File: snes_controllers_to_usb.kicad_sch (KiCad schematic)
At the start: 30 parts, among them J1 SNES_controller_port, J2 SNES_controller_port, J3 SNES_controller_port, J4 SNES_controller_port, Q1 BSS123, SW1 RST_PUSH, U1 PicoW

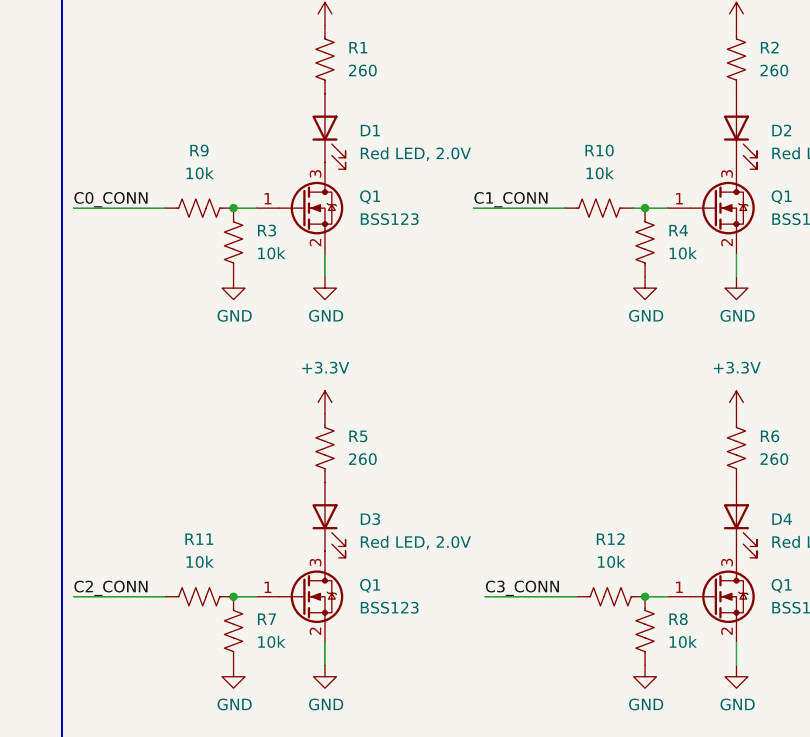
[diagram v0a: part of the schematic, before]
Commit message: Change transistor gate resistors to 1kOhm
 - Currently by using both 10kOhm resistors for pulldown and the current
   limiting resistor, it effectively makes a voltage divider, which sets
   the gate voltage a little low. Change the current limiting resistor
   to 1kOhm to make the gate voltage be 90% of the input voltage, which
   should be good enough.
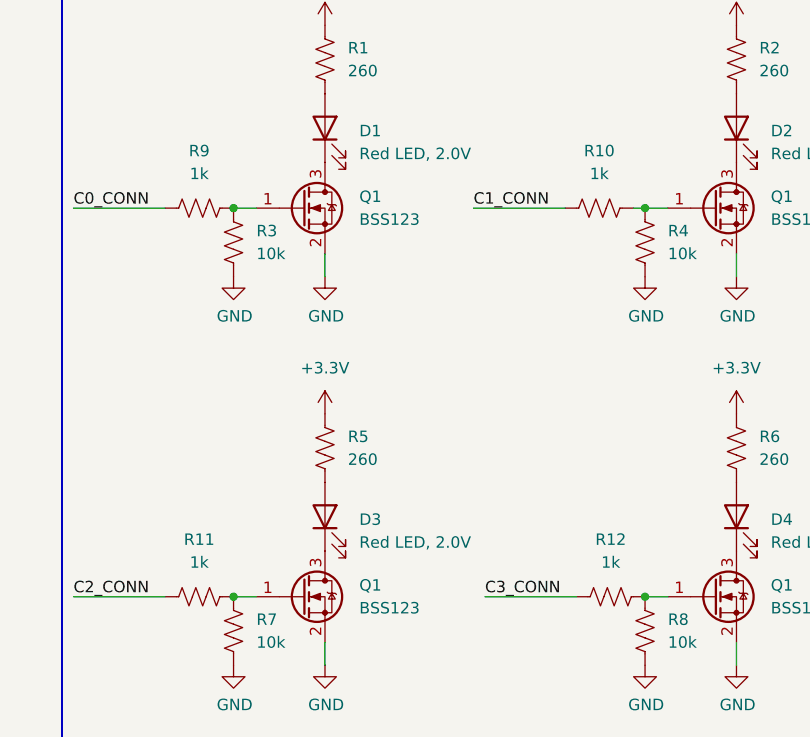
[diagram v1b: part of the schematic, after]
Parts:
- R10, R11, R12, R9: value 10k -> 1k
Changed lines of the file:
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@@
   (title_block
     (title "SNES Controllers to USB")
-    (date "2024-02-10")
-    (rev "A")
+    (date "2024-02-28")
+    (rev "B*")
     (comment 1 "Designed By: Gabriel Marcano")
   )
@@
       (effects (font (size 1.27 1.27)))
     )
-    (property "Value" "10k" (at 247.65 58.42 90)
+    (property "Value" "1k" (at 247.65 58.42 90)
       (effects (font (size 1.27 1.27)))
     )
@@
       (effects (font (size 1.27 1.27)))
     )
-    (property "Value" "10k" (at 203.2 101.6 90)
+    (property "Value" "1k" (at 203.2 101.6 90)
       (effects (font (size 1.27 1.27)))
     )
@@
       (effects (font (size 1.27 1.27)))
     )
-    (property "Value" "10k" (at 203.2 58.42 90)
+    (property "Value" "1k" (at 203.2 58.42 90)
       (effects (font (size 1.27 1.27)))
     )
@@
       (effects (font (size 1.27 1.27)))
     )
-    (property "Value" "10k" (at 248.92 101.6 90)
-      (effects (font (size 1.27 1.27)))
-    )
+    (property "Value" "1k" (at 248.92 101.6 90)
+      (effects (font (size 1.27 1.27)))
+    )

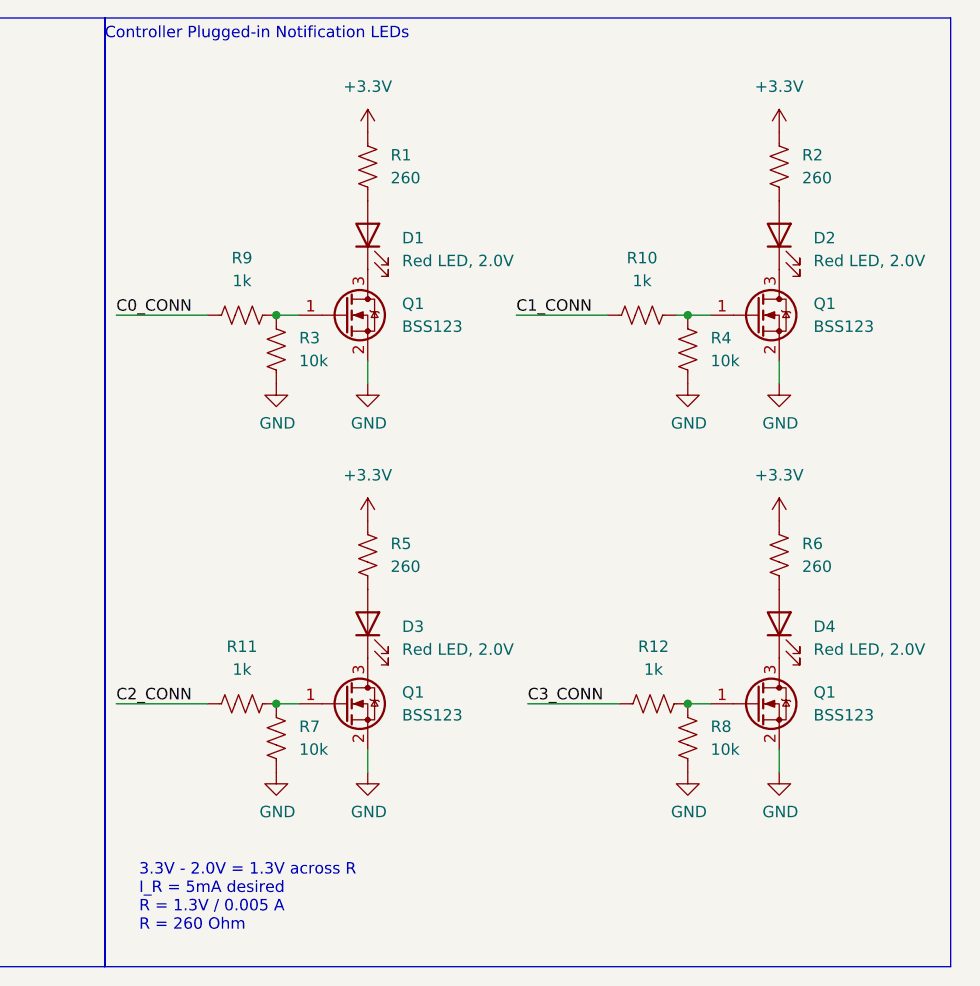
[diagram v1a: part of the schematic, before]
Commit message: Update to KiCAD 8, revision B, move some resistors
 - Update schematic and PCB to KiCAD8
 - Move R7, R8, R9, and R10 so they no longer make a voltage divider at
   the transistor bases
 - Updated drawings
 - Replaced SNES port footprint with one where the silkscreen doesn't go
   past the end of the board
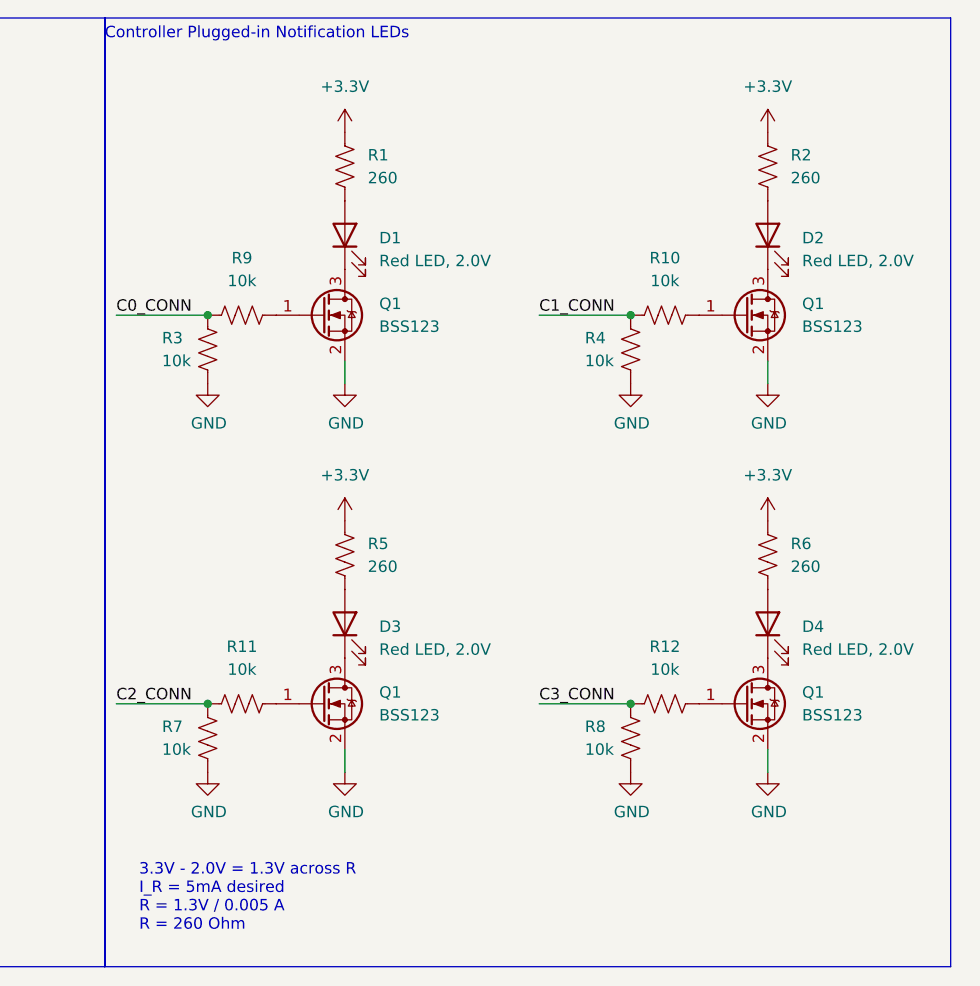
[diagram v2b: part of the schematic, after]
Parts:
- J1, J2, J3, J4: footprint Marcano:SNES_CONTROLLER_PORT_FEMALE -> Marcano:SNES_CONTROLLER_PORT_FEMALE_SHORT
- R10, R11, R12, R9: value 1k -> 10k
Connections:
- net C0_CONN: now also R3.1
- net C1_CONN: now also R4.1
- net C2_CONN: now also R7.1
- net C3_CONN: now also R8.1
- net at Q1.1 (G), R10.2: no longer R4.1
- net at Q1.1 (G), R11.2: no longer R7.1
- net at Q1.1 (G), R9.2: no longer R3.1
- net at Q1.1 (G), R12.2: no longer R8.1
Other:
- moved on the sheet: D1, D2, D3, D4, Q1, R1, R10, R12, R2, R5, R6
